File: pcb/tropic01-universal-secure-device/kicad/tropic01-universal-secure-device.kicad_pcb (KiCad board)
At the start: 4 copper layers, 42.7 x 36 mm, 90 parts, among them J1 USB4105-GF-A, J2 ER-TFT024IPS-3 50P FFC, J6 SM04B-SRSS-TB, J9 S2B-PH-SM4-TB, SW1 EVQP7J01P, U1 STM32U585VIT6, U10 BQ24074RGTR, U11 OPTIGA-TRUST-M-SLS32AIA, U13 TPS22917DBVR, U14 TPS22917DBVR, U15 TPS61165DBVR, U2 TR01-C2P-T301, U3 TPS62840DLCR, U4 TPS22917DBVR, U5 W25Q128JVSIQ, U7 TPD4E05U06DQAR, U8 TPS2553DBVR, U9 ST25R3916B-AQET, X1 16MHz, X3 FA-238 27.12MHz

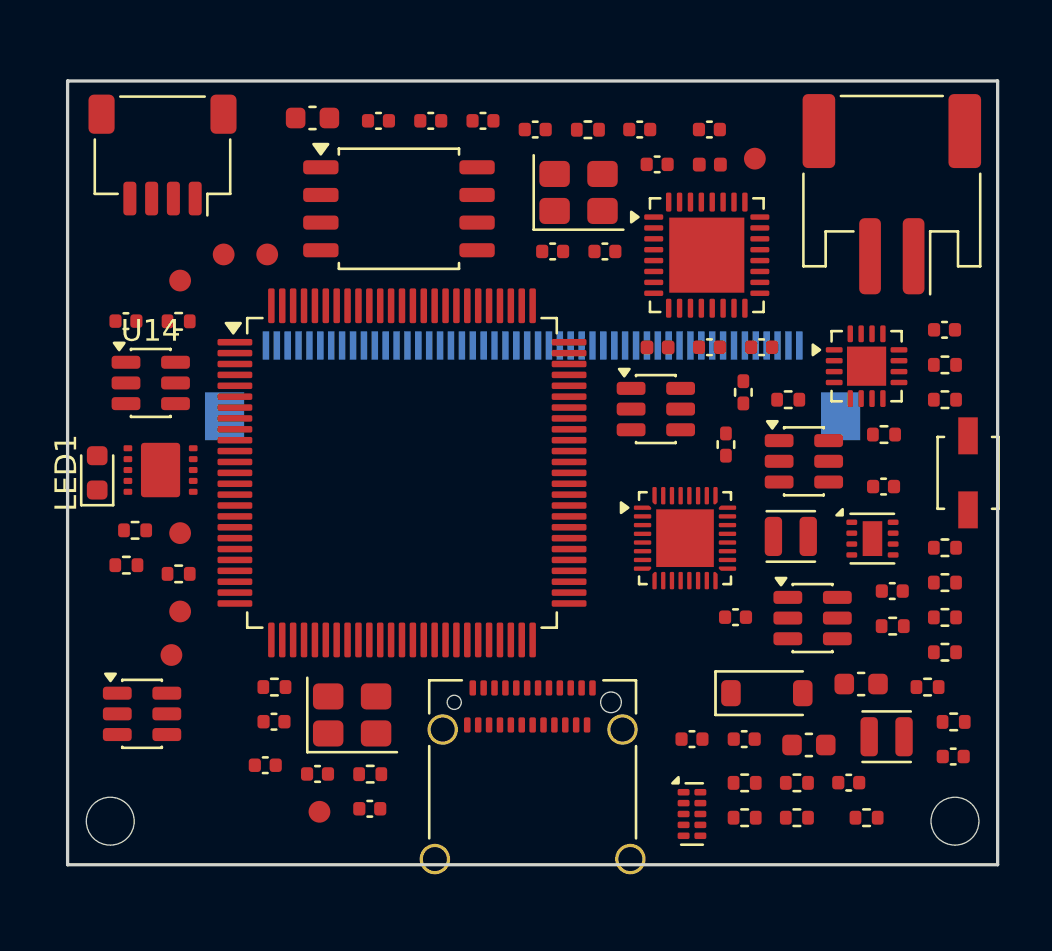
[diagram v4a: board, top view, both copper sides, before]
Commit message: feat(pcb): RGB status LED + grid-aligned placement tidy
Status LED: swap the single red LED for a discrete common-anode RGB
(Broadcom ASMB-MTB0-0A3A2, PLCC-4, top-view). Common anode -> SYS_PWR_IN
(~3.5-4.4V) so green/blue (Vf ~3.0-3.2V) have the drive headroom 3V3 lacks;
R/G/B cathodes via RLED1(470)/RLED2(220)/RLED3(220) -> LED_R/LED_G/LED_B on
3 STM32 GPIOs (active-low sink, PWM colour). Placed center-left opposite SW1,
top-emitting. Net wiring verified; 0 courtyard/clearance overlaps.

Placement: grid-snap all interior parts to 0.5mm + greedy overlap-resolve for
a tidier, axis-aligned layout; back side still carries only J2.

Contracts/docs: add status_led_rgb bus + notes to netlist-contract.json;
record rgb_status_led (physical pins 2/9/16, MCU pinmux datasheet-pending,
pin-2/BTN_RIGHT overlap flagged) in pinmux-ledger.json; update
component-decisions.md.

Known follow-ups (cosmetic / process, not blocking): silk reference cleanup
(done at final polish, after routing); MCU pinmux datasheet review for LED_R/G/B;
TFT_SPI_MISO left as a 1-pad net (display is write-only by design).
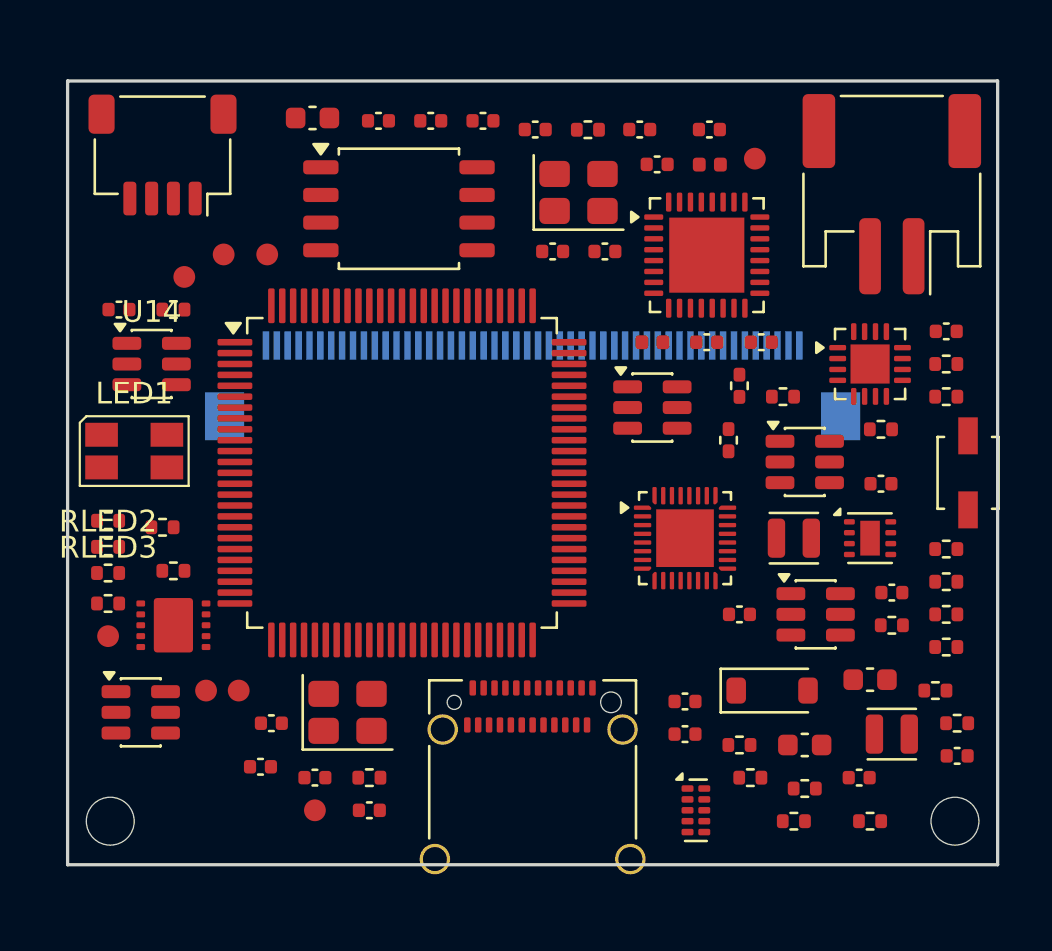
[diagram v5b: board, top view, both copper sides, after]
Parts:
- added RLED2: 220, R_0402_1005Metric, F.Cu at (12.5, 55.4)
- added RLED3: 220, R_0402_1005Metric, F.Cu at (12.5, 56.6)
- LED1: value KP-1608SURCK -> ASMB-MTB0-0A3A2; footprint LED_0603_1608Metric -> LED_Avago_PLCC4_3.2x2.8mm_CW
- RLED1: value 1k -> 470
- moved RLED1 10.8 mm to (12.5, 54.2)
- moved U11 7.15 mm to (15.5, 59.0)
- moved TP_BOOT0 5.77 mm to (12.5, 59.5)
- moved TP_NRST 3.82 mm to (17.0, 62.0)
- moved TP_SWDIO 3.50 mm to (18.5, 62.0)
- moved C4 3.22 mm to (39.0, 62.5)
- moved R1 3.16 mm to (41.5, 64.5)
- moved R4 3.07 mm to (44.5, 66.5)
- moved LED1 1.97 mm to (13.7, 51.0), turned to 0 degrees
- moved R6 1.95 mm to (12.5, 58.0)
- moved R22 1.27 mm to (15.0, 54.5)
- moved U14 0.87 mm to (14.5, 47.0)
- moved C7 0.62 mm to (13.0, 44.5)
- moved R7 0.59 mm to (15.5, 44.5)
- moved C6 0.53 mm to (47.0, 66.0)
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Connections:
- net LED_STATUS renamed LED_R
- LED1 pad 1: LED_STATUS_LED -> SYS_PWR_IN
- LED1 pad 2: GND -> LED_BK
- RLED1 pad 2: LED_STATUS_LED -> LED_RK
- U1 pad 16: (no net) -> LED_B
- U1 pad 9: (no net) -> LED_G

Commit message: feat(pcb): consolidate SWD onto one Tag-Connect TC2030 (J7)
Replace the 5 scattered SWD pads with a single Tag-Connect TC2030-NL footprint
(J7): pad1=SYS_3V3, 2=SWDIO, 3=NRST, 4=SWCLK, 5=GND (ARM SWD-on-TC2030 pinout).
Remove TP_SWDIO/TP_SWCLK/TP_NRST. The 7x4mm footprint did not fit any gap on the
68%-full board, so the movable parts were repacked around it (board is unrouted,
no routing lost). GND plane refilled to clear J7's NPTH holes. DRC: only the
accepted USB-C edge posts remain.
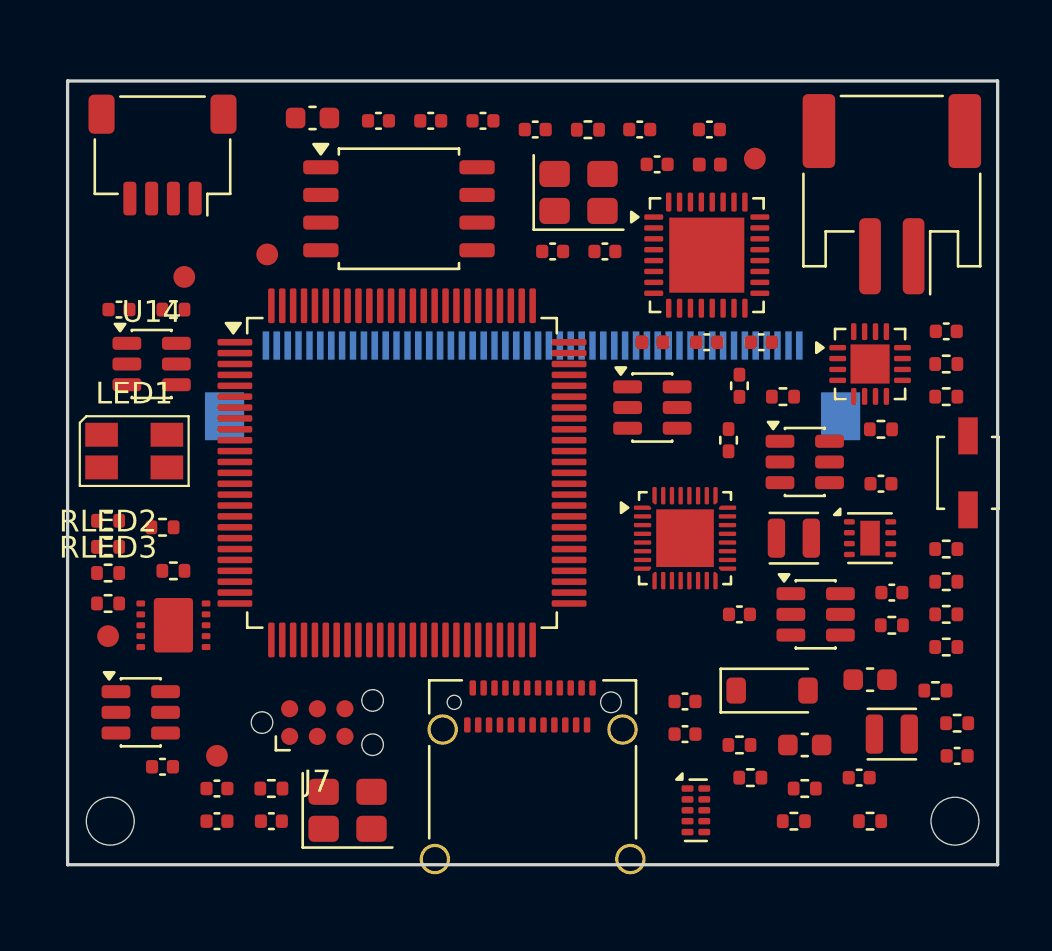
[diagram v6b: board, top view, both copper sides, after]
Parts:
- removed TP_NRST: NRST, TestPoint:TestPoint_Pad_D1.0mm
- removed TP_SWCLK: SWCLK, TestPoint:TestPoint_Pad_D1.0mm
- removed TP_SWDIO: SWDIO, TestPoint:TestPoint_Pad_D1.0mm
- added J7: SWD_TC2030, Tag-Connect_TC2030-IDC-NL_2x03_P1.27mm_Vertical, F.Cu at (22.1, 63.5)
- moved C19 7.02 mm to (15.0, 65.5)
- moved C18 5.15 mm to (17.5, 68.0)
- moved TP_GND 5.15 mm to (17.5, 65.0)
- moved C17 4.53 mm to (20.0, 68.0)
- moved R5 4.53 mm to (20.0, 66.5)
- moved X1 4.50 mm to (23.5, 67.5)
- moved C16 2.24 mm to (17.5, 66.5)
